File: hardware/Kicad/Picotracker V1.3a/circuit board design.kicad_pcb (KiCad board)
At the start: 2 copper layers, 33.3 x 20.1 mm, 39 parts, among them J1 Conn_01x10, J2 GND, J3 3.3V, J4 ICSS Logo, J5 Conn_01x01, Q1 IRLML6402, U1 MAX-M8C, U3 CMWX1ZZABZ-078, U6 MS5607-02BA

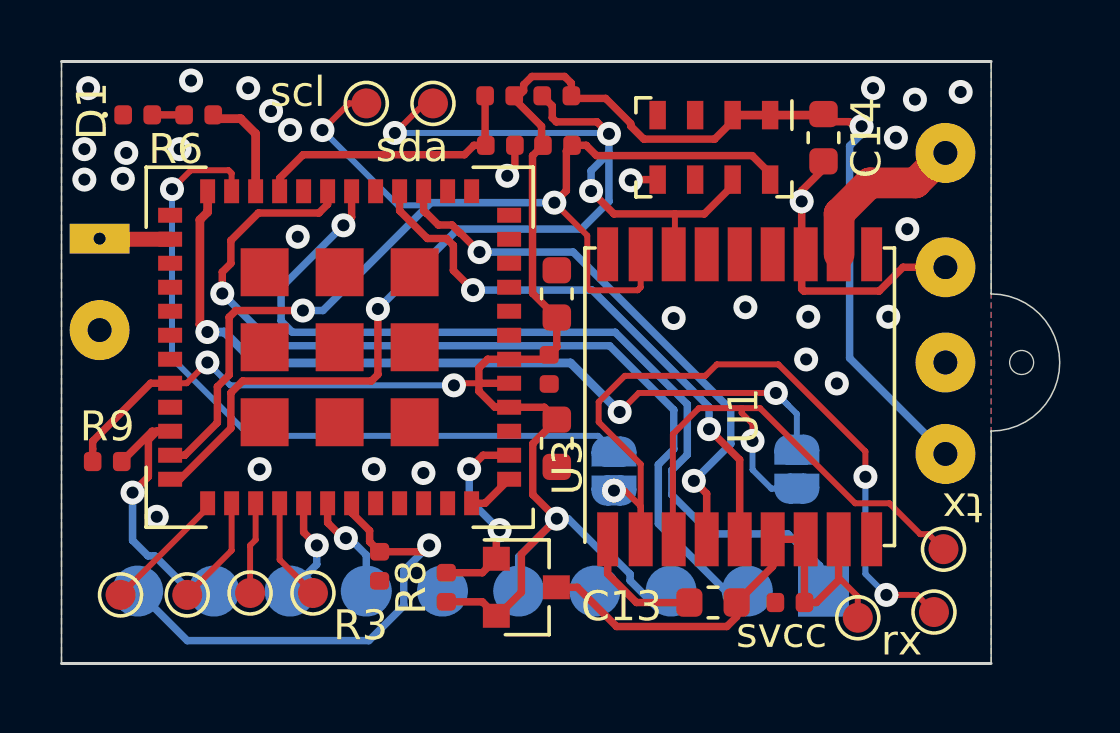
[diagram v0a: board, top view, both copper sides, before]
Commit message: Change GPS antenna pad to the same as the lora pad
Use a rectangular pad for GPS antenna. Much stronger connection.
Put in test pad on GPS timepulse.
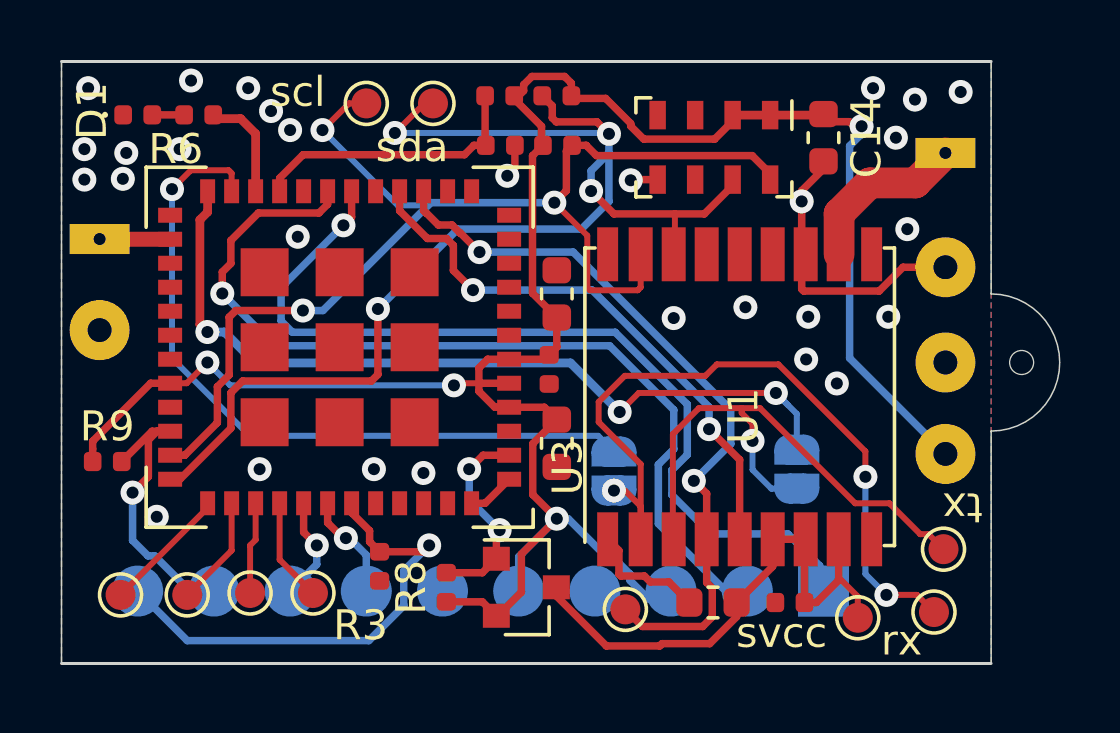
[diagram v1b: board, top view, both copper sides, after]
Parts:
- added TP10: TestPoint, TestPoint:TestPoint_Pad_D1.0mm, F.Cu at (285.5, 178.3)
- AE1: value Lora Antenna -> GPS Antenna; footprint pico_tracker:SolderWirePad_1x01_Drill0.8mm_square -> pico_tracker:custom_antenna_pad
- AE2: footprint Connector_Wire:SolderWirePad_1x01_Drill0.8mm -> pico_tracker:custom_antenna_pad
- turned AE2 to 180 degrees
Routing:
- net /GPS_TIMEPULSE: track 18.6 -> 24.6 mm
- net Net-(C12-Pad1): track 18.7 -> 19.4 mm
